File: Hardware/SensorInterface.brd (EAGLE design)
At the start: 69 x 20 mm, 73 parts, among them J3 CONN_32.54_SCREW, J4 CONN_32.54_SCREW, J5 CONN_42.54_SCREW, Q1 DMG3404, Q2 DMG3404, Q3 DMG3404, Q4 DMG3404, Q5 DMG3404, U10 SN74AHC1G86DCK, U11 MCP6041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

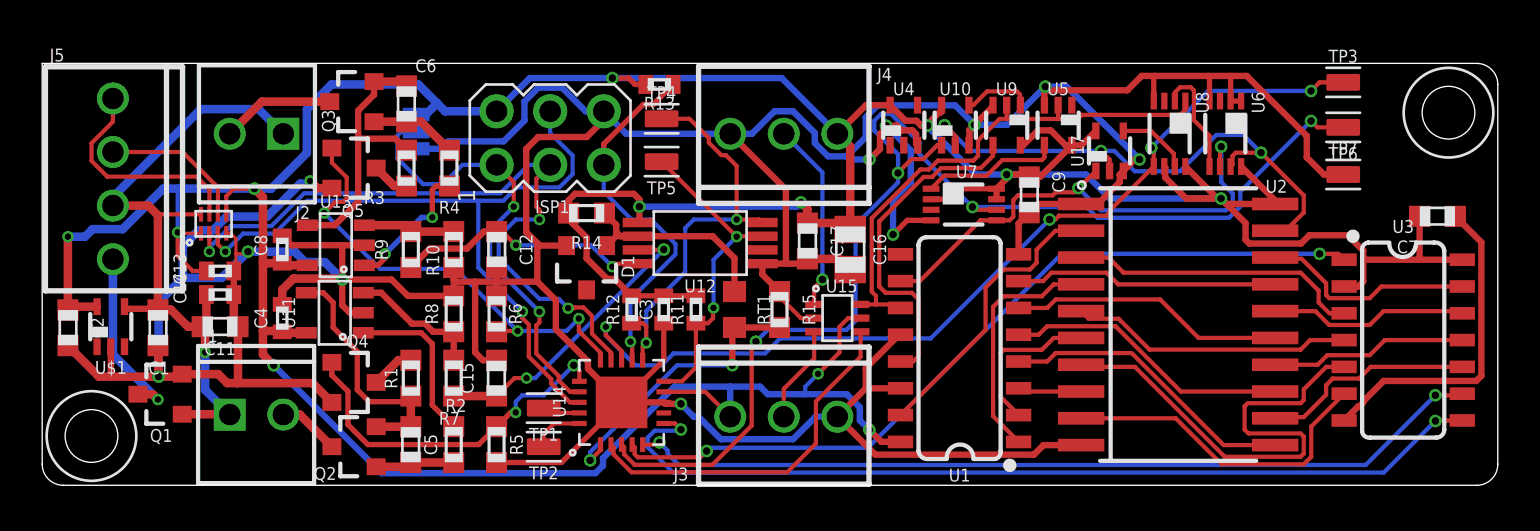
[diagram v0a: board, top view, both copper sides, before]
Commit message: Layout cleanup ready for review
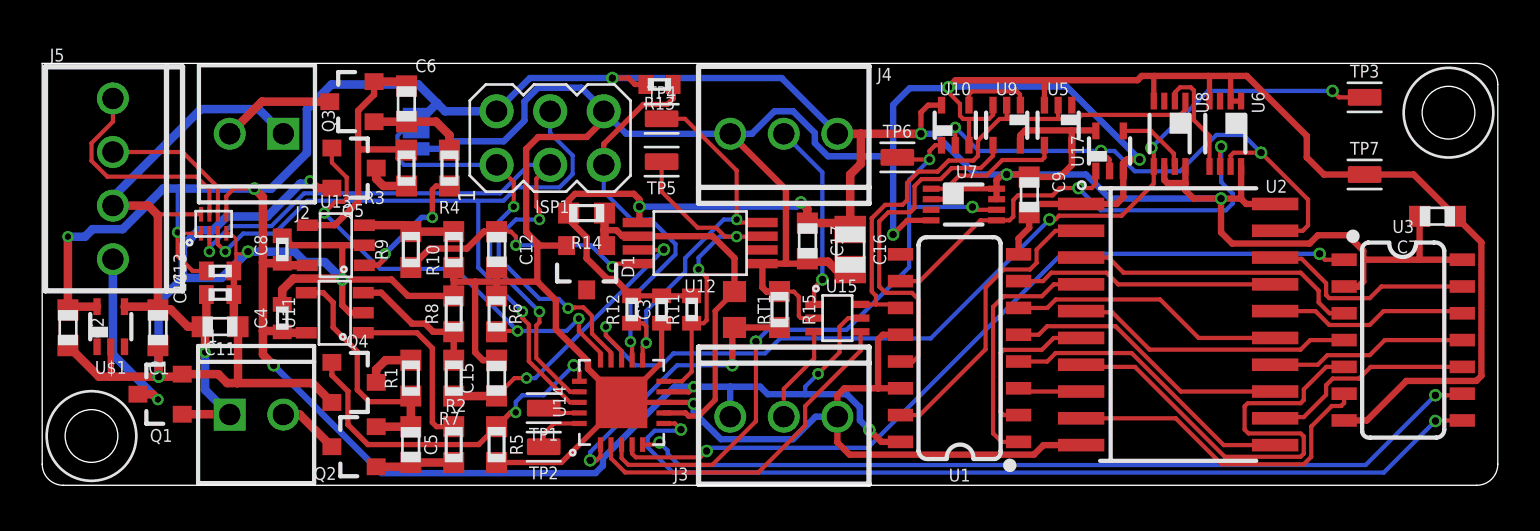
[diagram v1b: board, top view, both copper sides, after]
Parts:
- removed U4: (no value), bschulz:DCK_R-PDSO-G5
- moved TP6 21.2 mm to (40.5, 15.5), turned to 0 degrees
- moved LOGO1 5.75 mm to (60.9, 5.18)
- moved TP3 1.24 mm to (62.7, 18.4)
- moved TP7 1.02 mm to (62.7, 14.7)
- moved R11 0.20 mm to (30.8, 8.33)
- moved C3 0.10 mm to (29.4, 8.33)
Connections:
- net 3V3: no longer U4.5
- net GND: no longer U4.3
- net VREF: now also U14.7
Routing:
- net URES: track 58.5 -> 32.9 mm, vias 4 -> 3
- net GND: track 260.3 -> 270.7 mm, vias 11 -> 8
- net VREF: track 9.66 -> 18.2 mm
- net 3V3: track 211.7 -> 208.5 mm, vias 12 -> 13
- net SCL: track 15.4 -> 17.0 mm
- net !INT: track 44.2 -> 45.5 mm
- net SDA: track 19.7 -> 18.6 mm
- net ADR_SEL: track 21.3 -> 20.6 mm
- net F_IN_SW: track 17.2 -> 16.6 mm
- net RCLK: track 16.0 -> 16.6 mm
- net N$1: track 13.7 -> 14.3 mm
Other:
- board text added: "ADR0"
- board text added: "ADR1"
- board text added: "JP1"
- board text added: "Project Calypso v0.1.0 2019.02.04 Bobby Schulz (schematic) Andy Wickert and Bobby Schulz (layout) UMN senior design team (basis design) Design: Northern Widget LLC in collaboration with The University of Minnesota"
- board text removed: "Project Calypso v0.0.0 2018.12.23 and 2019.01.01 Bobby Schulz (schematic) Andy Wickert and Bobby Schulz (layout) UMN senior design team (basis design) Design: Northern Widget LLC in collaboration with The University of Minnesota"

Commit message: SE corner hole added
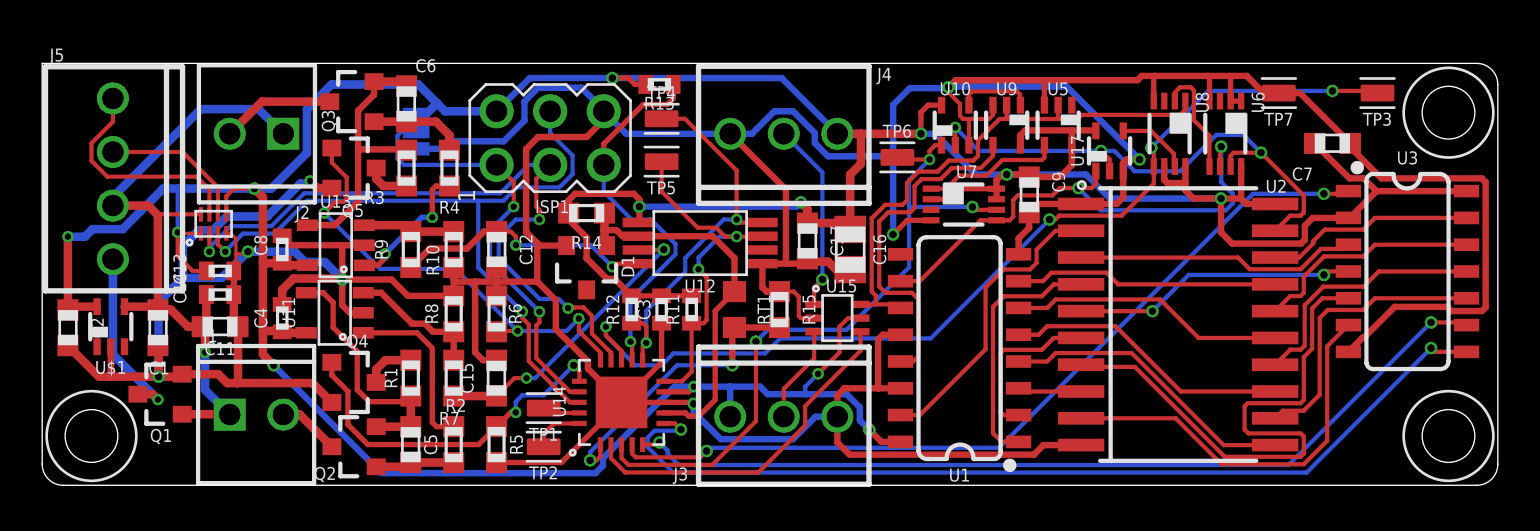
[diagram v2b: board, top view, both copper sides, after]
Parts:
- added H3: (no value), bschulz:2_56
- moved LOGO1 20.0 mm to (41.4, 9.65)
- moved C7 6.06 mm to (61.2, 16.2)
- moved TP7 5.61 mm to (58.6, 18.6), turned to 180 degrees
- moved U3 3.26 mm to (64.7, 10.8)
- moved TP3 0.64 mm to (63.3, 18.6), turned to 180 degrees
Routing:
- net N$11: track 23.1 -> 26.6 mm
- net N$13: track 10.1 -> 13.6 mm
- net N$12: track 15.9 -> 18.9 mm
- net N$14: track 9.35 -> 12.0 mm
- net CLK: track 43.3 -> 44.9 mm
- net !CLEAR: track 40.8 -> 42.5 mm
- net GND: track 270.7 -> 269.1 mm
- net N$15: track 9.45 -> 10.8 mm
- net DATA: track 38.4 -> 39.7 mm
- net !P=Q: track 26.4 -> 25.8 mm
- net !INT: track 45.5 -> 46.1 mm
- net N$9: track 13.9 -> 13.4 mm
- net N$10: track 13.4 -> 13.5 mm, vias 0 -> 2

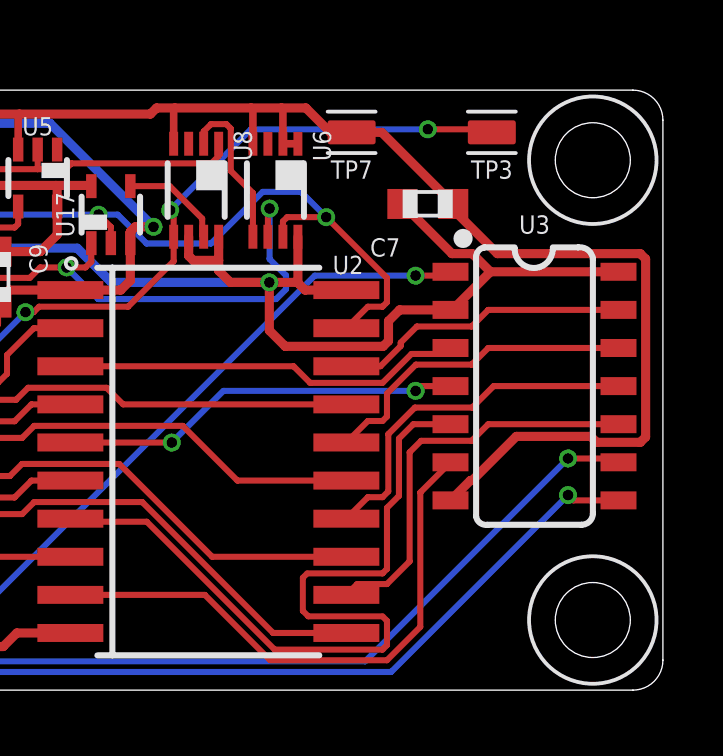
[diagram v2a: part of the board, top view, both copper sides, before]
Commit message: Minor cleanup, generated gerbers
Cleaned up silkscreen on board and generated gerbers for main board and breakouts
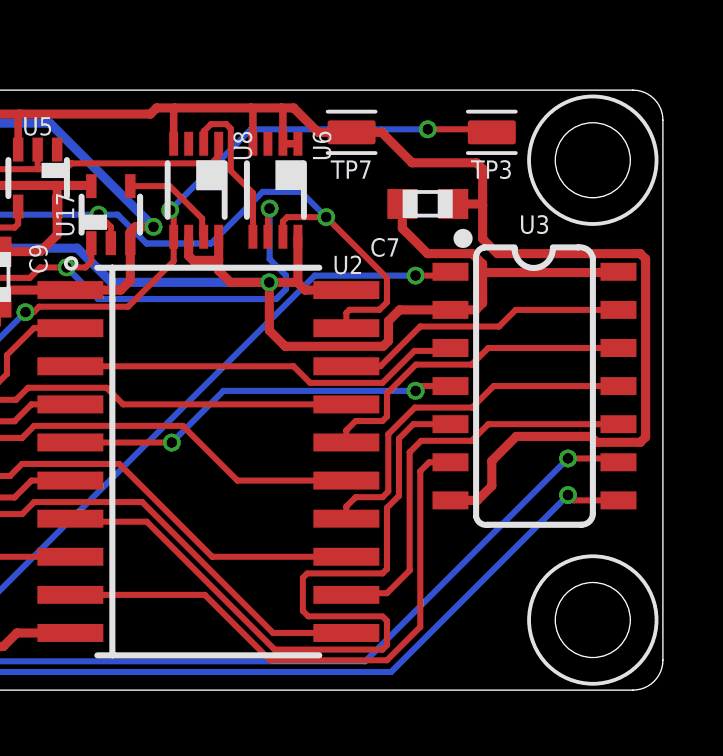
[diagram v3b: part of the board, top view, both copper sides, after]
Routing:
- net GND: track 269.1 -> 271.7 mm
- net 3V3: track 208.9 -> 210.0 mm
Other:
- board text removed: "ADR0"
- board text removed: "ADR1"
- board text removed: "JP1"

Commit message: Added PDFs and replaced OSHW logo
Added PDFs for board (clean) and schematic (nearly clean), also replaced the OSHW logo with one from ColdSilicon which uses the correct layer
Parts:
- LOGO1: device SparkFun-Aesthetics:OSHW-LOGO-M -> bschulz:OSHW-LOGO-M
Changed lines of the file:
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@@
 <layer number="14" name="Route14" color="1" fill="6" visible="no" active="no"/>
 <layer number="15" name="Route15" color="4" fill="6" visible="no" active="no"/>
-<layer number="16" name="Bottom" color="1" fill="1" visible="yes" active="yes"/>
+<layer number="16" name="Bottom" color="1" fill="1" visible="no" active="yes"/>
 <layer number="17" name="Pads" color="2" fill="1" visible="yes" active="yes"/>
 <layer number="18" name="Vias" color="2" fill="1" visible="yes" active="yes"/>
 <layer number="19" name="Unrouted" color="6" fill="1" visible="yes" active="yes"/>
 <layer number="20" name="Dimension" color="24" fill="1" visible="yes" active="yes"/>
-<layer number="21" name="tPlace" color="7" fill="1" visible="yes" active="yes"/>
-<layer number="22" name="bPlace" color="7" fill="1" visible="yes" active="yes"/>
-<layer number="23" name="tOrigins" color="15" fill="1" visible="yes" active="yes"/>
-<layer number="24" name="bOrigins" color="15" fill="1" visible="yes" active="yes"/>
-<layer number="25" name="tNames" color="7" fill="1" visible="yes" active="yes"/>
-<layer number="26" name="bNames" color="7" fill="1" visible="yes" active="yes"/>
+<layer number="21" name="tPlace" color="7" fill="1" visible="no" active="yes"/>
+<layer number="22" name="bPlace" color="7" fill="1" visible="no" active="yes"/>
+<layer number="23" name="tOrigins" color="15" fill="1" visible="no" active="yes"/>
+<layer number="24" name="bOrigins" color="15" fill="1" visible="no" active="yes"/>
+<layer number="25" name="tNames" color="7" fill="1" visible="no" active="yes"/>
+<layer number="26" name="bNames" color="7" fill="1" visible="no" active="yes"/>
 <layer number="27" name="tValues" color="7" fill="1" visible="no" active="yes"/>
 <layer number="28" name="bValues" color="7" fill="1" visible="no" active="yes"/>
@@
 <layer number="38" name="bTest" color="7" fill="1" visible="no" active="yes"/>
 <layer number="39" name="tKeepout" color="4" fill="11" visible="yes" active="yes"/>
-<layer number="40" name="bKeepout" color="1" fill="11" visible="yes" active="yes"/>
+<layer number="40" name="bKeepout" color="1" fill="11" visible="no" active="yes"/>
 <layer number="41" name="tRestrict" color="4" fill="10" visible="yes" active="yes"/>
-<layer number="42" name="bRestrict" color="1" fill="10" visible="yes" active="yes"/>
+<layer number="42" name="bRestrict" color="1" fill="10" visible="no" active="yes"/>
 <layer number="43" name="vRestrict" color="2" fill="10" visible="no" active="yes"/>
 <layer number="44" name="Drills" color="7" fill="1" visible="no" active="yes"/>
@@
 <layer number="49" name="Reference" color="7" fill="1" visible="no" active="yes"/>
 <layer number="50" name="dxf" color="7" fill="1" visible="no" active="no"/>
-<layer number="51" name="tDocu" color="7" fill="1" visible="yes" active="yes"/>
-<layer number="52" name="bDocu" color="7" fill="1" visible="yes" active="yes"/>
+<layer number="51" name="tDocu" color="7" fill="1" visible="no" active="yes"/>
+<layer number="52" name="bDocu" color="7" fill="1" visible="no" active="yes"/>
 <layer number="53" name="tGND_GNDA" color="7" fill="1" visible="no" active="no"/>
 <layer number="54" name="bGND_GNDA" color="7" fill="1" visible="no" active="no"/>
@@
 <attribute name="NAME" x="37.8968" y="9.4488" size="0.6096" layer="25" font="vector" ratio="15" align="center"/>
 </element>
-<element name="LOGO1" library="SparkFun-Aesthetics" package="OSHW-LOGO-M" value="OSHW-LOGOM" x="41.3512" y="9.652" smashed="yes" rot="MR0"/>
+<element name="LOGO1" library="bschulz" package="OSHW-LOGO-M" package3d_urn="urn:adsk.eagle:package:37126/1" value="OSHW-LOGOM" x="41.3512" y="9.652" smashed="yes" rot="MR0"/>
 <element name="U16" library="bschulz" package="DQM_R-PX2SON-N8" value="TXS0102DQM" x="8.128" y="12.3952" smashed="yes">
 <attribute name="DIGIKEY" value="296-28435-1-ND" x="8.128" y="18.9992" size="1.778" layer="27" display="off"/>
